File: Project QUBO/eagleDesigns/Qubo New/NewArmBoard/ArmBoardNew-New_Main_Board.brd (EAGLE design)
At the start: 114.3 x 114.3 mm, 13 parts, among them U1 BME280

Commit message: Prolly random fixes
I don't remember but it's probaly pretty good
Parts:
- moved JP1 7.66 mm to (20.3, 75.4)
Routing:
- net DGND: track 66.7 -> 59.6 mm
- net 5V: track 50.5 -> 47.6 mm
- added copper zone on layer 16, net N$1
- removed copper zone on layer 16, net DGND
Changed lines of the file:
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@@
 <text x="63.373" y="3.175" size="1.4224" layer="27" rot="R90">NC</text>
 <text x="65.786" y="3.175" size="1.4224" layer="27" rot="R90">NC</text>
-<text x="102.489" y="19.939" size="1.778" layer="21" rot="R90">ARM Shim Board
+<text x="34.925" y="19.431" size="1.778" layer="21" rot="R180">ARM Shim Board
 Rev 1.0
 Brendan Kane and Alex Jiao
 R@M 2018</text>
+<hole x="6.35" y="81.28" drill="3.302"/>
+<hole x="6.35" y="33.02" drill="3.302"/>
+<hole x="107.95" y="33.02" drill="3.302"/>
+<hole x="107.95" y="81.28" drill="3.302"/>
 </plain>
 <attributes>
@@
 <element name="R11" library="resistor" library_urn="urn:adsk.eagle:library:348" package="R0805" package3d_urn="urn:adsk.eagle:package:26059/1" value="5k" x="20.32" y="68.961"/>
 <element name="R17" library="resistor" library_urn="urn:adsk.eagle:library:348" package="R0805" package3d_urn="urn:adsk.eagle:package:26059/1" value="5k" x="84.709" y="42.799"/>
-<element name="JP1" library="pinhead" package="1X02" value="" x="12.7" y="76.2" rot="R90"/>
+<element name="JP1" library="pinhead" package="1X02" value="" x="20.32" y="75.438" rot="R90"/>
 </elements>
 <signals>
@@
 <wire x1="18.989" y1="60.706" x2="18.989" y2="57.023" width="0.254" layer="1"/>
 <wire x1="18.989" y1="57.023" x2="19.497" y2="56.515" width="0.254" layer="1"/>
-<wire x1="19.1465" y1="45.5625" x2="19.243" y2="45.466" width="0.254" layer="1"/>
 <wire x1="18.989" y1="49.657" x2="18.989" y2="45.72" width="0.254" layer="1"/>
-<wire x1="18.989" y1="45.72" x2="19.1465" y2="45.5625" width="0.254" layer="1"/>
+<wire x1="18.989" y1="45.72" x2="19.243" y2="45.466" width="0.254" layer="1"/>
 <wire x1="19.497" y1="56.515" x2="19.497" y2="50.165" width="0.254" layer="1"/>
 <wire x1="19.497" y1="50.165" x2="18.989" y2="49.657" width="0.254" layer="1"/>
@@
 <wire x1="20.50426875" y1="69.9904" x2="32.3716" y2="69.9904" width="0.254" layer="1"/>
 <wire x1="32.3716" y1="69.9904" x2="34.925" y2="67.437" width="0.254" layer="1"/>
-<wire x1="12.7" y1="74.93" x2="18.669" y2="68.961" width="0.254" layer="1"/>
 <wire x1="18.669" y1="68.961" x2="19.37" y2="68.961" width="0.254" layer="1"/>
 <polygon width="0.254" layer="1">
-<vertex x="6.604" y="76.2"/>
 <vertex x="12.7" y="70.104"/>
 <vertex x="12.7" y="38.1"/>
@@
 <vertex x="33.528" y="55.372"/>
 </polygon>
+<wire x1="19.37" y1="68.961" x2="19.37" y2="73.218" width="0.254" layer="1"/>
+<wire x1="19.37" y1="73.218" x2="20.32" y2="74.168" width="0.254" layer="1"/>
 </signal>
 <signal name="RES">
@@
 <contactref element="JP1" pad="2"/>
 <wire x1="50.8" y1="76.2976" x2="51.8886" y2="76.2976" width="0.254" layer="1"/>
-<polygon width="0.1524" layer="16">
-<vertex x="6.096" y="3.556"/>
-<vertex x="6.604" y="3.048"/>
-<vertex x="107.696" y="3.048"/>
-<vertex x="109.728" y="5.08"/>
-<vertex x="94.996" y="19.812"/>
-<vertex x="94.996" y="89.408"/>
-<vertex x="6.604" y="89.408"/>
-</polygon>
 <wire x1="50.8" y1="76.2976" x2="50.8" y2="78.232" width="0.254" layer="1"/>
 <wire x1="50.8" y1="78.232" x2="55.118" y2="78.232" width="0.254" layer="1"/>
@@
 <wire x1="68.58" y1="76.962" x2="55.118" y2="76.962" width="0.254" layer="1"/>
 <wire x1="33.4264" y1="66.3956" x2="34.925" y2="64.897" width="0.254" layer="16"/>
-<wire x1="31.50726875" y1="66.3956" x2="33.4264" y2="66.3956" width="0.254" layer="16"/>
-<wire x1="12.7" y1="77.47" x2="20.43286875" y2="77.47" width="0.254" layer="16"/>
-<wire x1="20.43286875" y1="77.47" x2="31.50726875" y2="66.3956" width="0.254" layer="16"/>
+<wire x1="33.4264" y1="66.3956" x2="31.50726875" y2="66.3956" width="0.254" layer="16"/>
+<wire x1="20.32" y1="76.708" x2="20.43286875" y2="77.47" width="0.254" layer="16"/>
 <wire x1="50.8" y1="76.2976" x2="48.3576" y2="76.2976" width="0.254" layer="1"/>
 <wire x1="48.3576" y1="76.2976" x2="48.26" y2="76.2" width="0.254" layer="1"/>
 <via x="48.26" y="76.2" extent="1-16" drill="0.35"/>
+<wire x1="31.50726875" y1="66.3956" x2="21.19486875" y2="76.708" width="0.254" layer="16"/>
+<wire x1="21.19486875" y1="76.708" x2="20.32" y2="76.708" width="0.254" layer="16"/>
+<wire x1="34.925" y1="64.897" x2="48.26" y2="76.2" width="0" layer="19" extent="1-1"/>
 </signal>
 <signal name="CANTX">
@@
 <contactref element="U$3" pad="2-2"/>
 </signal>
+<signal name="N$1">
+<polygon width="0.254" layer="16">
+<vertex x="12.7" y="76.2"/>
+<vertex x="13.462" y="6.604"/>
+<vertex x="89.662" y="6.604"/>
+<vertex x="90.424" y="7.366"/>
+<vertex x="90.424" y="77.216"/>
+<vertex x="88.9" y="78.74"/>
+<vertex x="16.002" y="78.74"/>
+<vertex x="13.462" y="76.2"/>
+</polygon>
+</signal>
 </signals>

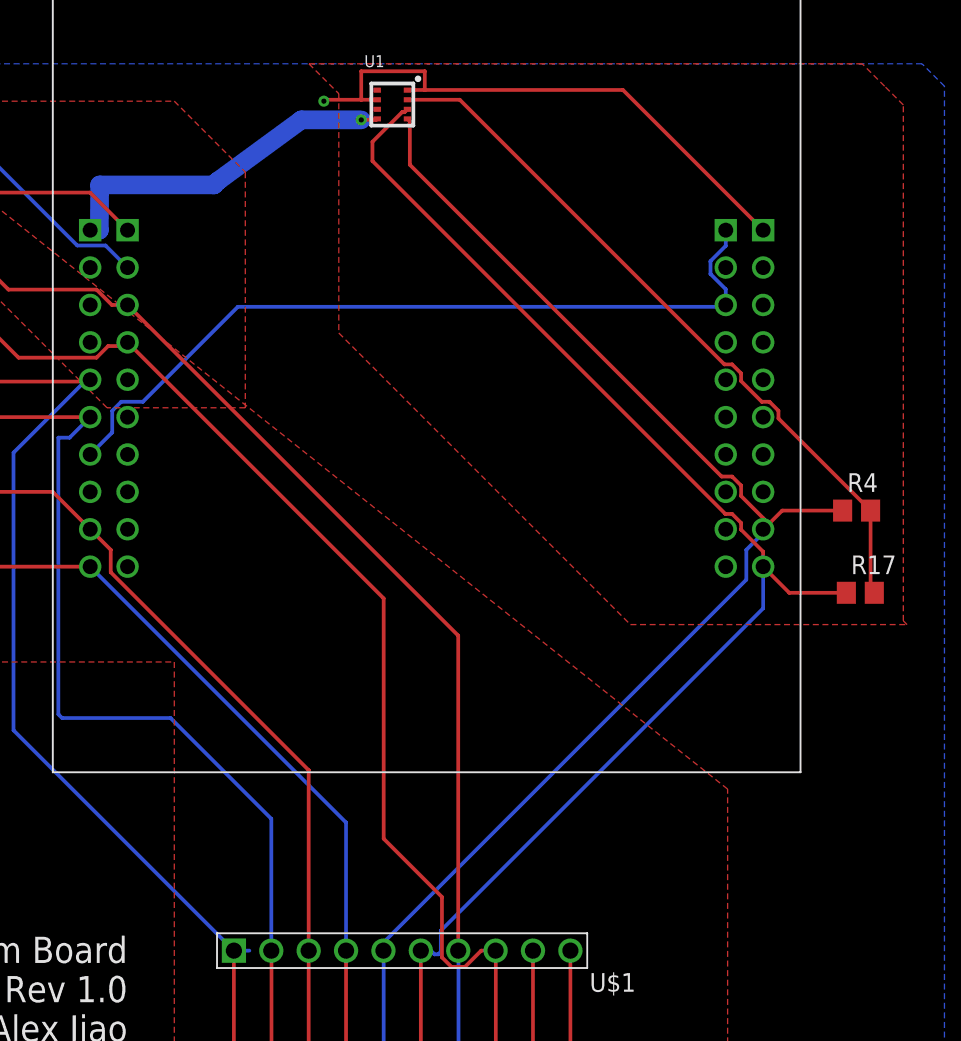
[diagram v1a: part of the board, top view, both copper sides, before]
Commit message: Fixes to TIVA board
Some of the pins were named wrong so I fixed them
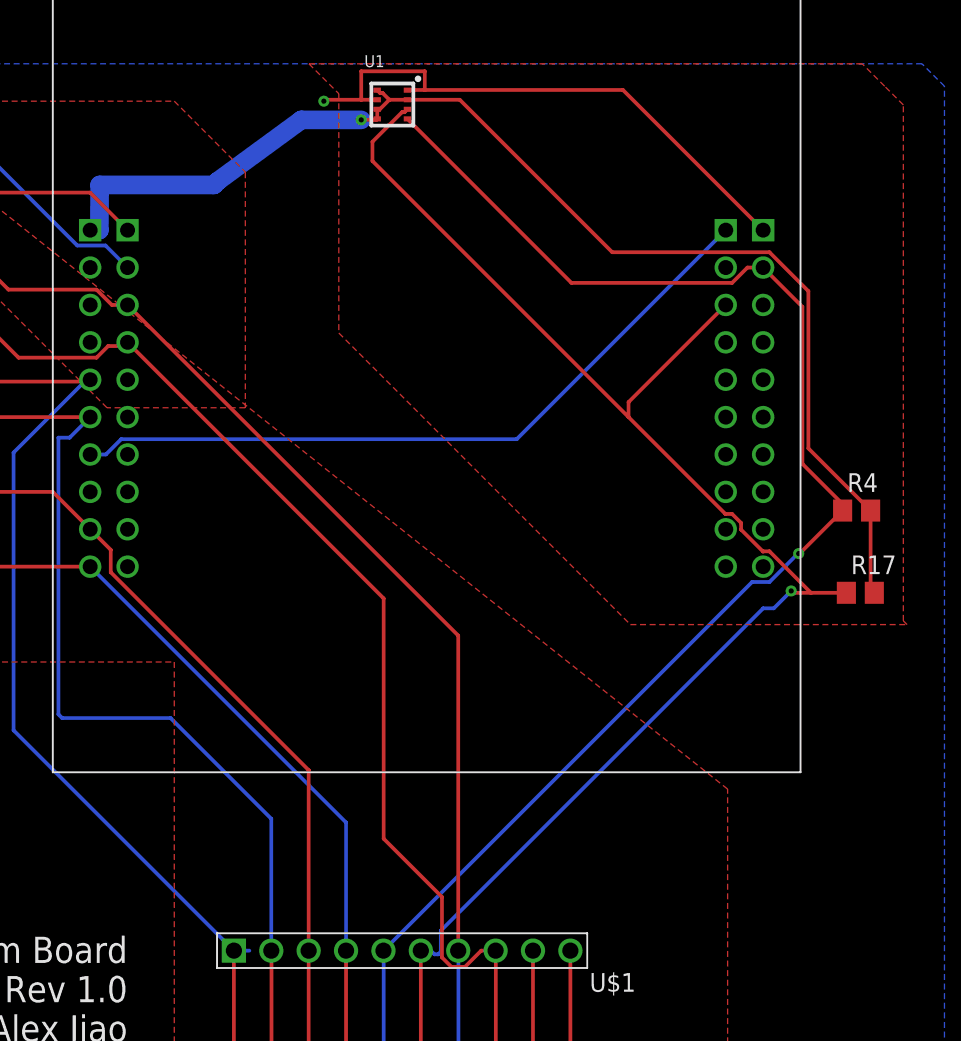
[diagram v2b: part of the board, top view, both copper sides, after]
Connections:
- net CANTX renamed CS
- net CTS_MF renamed MOSI_1
- net PB5 renamed CS_2
- net RTS_MF renamed MISO_1
- removed net PB2: U$3.2-2
- new net CS_0: U$3.2-9
- new net MISO_0: U$3.2-8
- new net MISO_3: U$3.3-5
- new net MOSI_0: U$3.1-8
- new net MOSI_3: U$3.3-6
- new net SCK_0: U$3.2-10
- net SCL_0: now also U$3.2-2; no longer U$3.2-9
- net SDA_0: now also U$3.4-3; no longer U$3.2-10
- net SPI_CLK: no longer U$3.4-3
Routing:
- net SDA_0: track 94.9 -> 105.7 mm, vias 0 -> 1
- net 3.3V: track 73.7 -> 83.5 mm
- net SCL_0: track 92.0 -> 100.0 mm, vias 0 -> 1
- net SPI_CLK: track 54.2 -> 49.5 mm
- added copper zone on layer 16, net DGND
- removed copper zone on layer 16, net N$1

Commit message: Changes to Tiva board
I had to rewire some things
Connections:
- new net SPI_CLK_2: U$3.1-7
- net 3.3V: now also R15.1, R16.1, U$1.P$9; no longer R17.2, R4.2
- net 5V: now also R17.2, R4.2; no longer R15.1, R16.1
- net N$9: no longer U$1.P$9
- net SCL_0: no longer U1.P$4
- net SCL_1: now also U1.P$4
- net SDA_0: no longer U1.P$3
- net SDA_1: now also U1.P$3
- net SPI_CLK: no longer U$3.1-7
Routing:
- net 3.3V: track 83.5 -> 180.6 mm, vias 1 -> 2
- net 5V: track 47.6 -> 109.2 mm
- net SPI_CLK: track 49.5 -> 0.00 mm
- net SDA_1: track 54.5 -> 101.0 mm, vias 0 -> 1
- net SCL_1: track 55.7 -> 94.1 mm, vias 0 -> 2
- net SCL_0: track 100.0 -> 70.8 mm
- net N$9: track 8.34 -> 0.02 mm
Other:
- board size 114.3 x 114.3 mm -> 114.3 x 88.9 mm
- board text added: "VV this side down VV"

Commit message: armboard modifications
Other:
- board size 114.3 x 88.9 mm -> 96.8 x 89.2 mm
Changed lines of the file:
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@@
 <?xml version="1.0" encoding="utf-8"?>
 <!DOCTYPE eagle SYSTEM "eagle.dtd">
-<eagle version="8.6.0">
+<eagle version="9.3.1">
 <drawing>
 <settings>
@@
 <text x="42.545" y="3.175" size="1.4224" layer="21" rot="R90">SCL_2</text>
 <wire x1="0" y1="88.9" x2="0" y2="0" width="0.1524" layer="20"/>
-<wire x1="0" y1="0" x2="114.3" y2="0" width="0.1524" layer="20"/>
-<wire x1="114.3" y1="0" x2="114.3" y2="88.9" width="0.1524" layer="20"/>
-<wire x1="114.3" y1="88.9" x2="0" y2="88.9" width="0.1524" layer="20"/>
+<wire x1="0" y1="0" x2="96.774" y2="-0.254" width="0.1524" layer="20"/>
+<wire x1="96.774" y1="-0.254" x2="96.774" y2="88.646" width="0.1524" layer="20"/>
+<wire x1="96.774" y1="88.646" x2="0" y2="88.9" width="0.1524" layer="20"/>
 <text x="45.085" y="3.175" size="1.4224" layer="21" rot="R90">SDA_2</text>
 <text x="47.752" y="3.175" size="1.4224" layer="21" rot="R90">SCL_1</text>
@@
 <hole x="6.35" y="81.28" drill="3.302"/>
 <hole x="6.35" y="33.02" drill="3.302"/>
-<hole x="107.95" y="33.02" drill="3.302"/>
-<hole x="107.95" y="81.28" drill="3.302"/>
-<text x="88.9" y="0" size="1.778" layer="121">VV this side down VV</text>
+<hole x="88.9" y="33.02" drill="3.302"/>
+<hole x="88.9" y="81.28" drill="3.302"/>
+<text x="63.5" y="0" size="1.778" layer="121">VV this side down VV</text>
 </plain>
 <attributes>
@@
 <param name="checkStop" value="0"/>
 <param name="checkValues" value="0"/>
+<param name="checkNames" value="1"/>
+<param name="checkWireStubs" value="1"/>
+<param name="checkPolygonWidth" value="0"/>
 <param name="useDiameter" value="13"/>
 <param name="maxErrors" value="50"/>
@@
 </autorouter>
 <elements>
-<element name="U1" library="BME280ComponentLibrary" package="BME280_LGA" value="BME280" x="52.9136" y="75.9726">
+<element name="U1" library="BME280ComponentLibrary" package="BME280_LGA" value="BME280" x="52.9136" y="75.9726" smashed="yes">
+<attribute name="NAME" x="51.0086" y="78.5126" size="0.8128" layer="25" font="vector"/>
 <attribute name="PROD_ID" value="IC-13090" x="52.9136" y="75.9726" size="1.778" layer="27" display="off"/>
+<attribute name="VALUE" x="51.0086" y="72.7976" size="0.8128" layer="27" font="vector"/>
 </element>
 <element name="U$1" library="molex" package="KK254_10-PIN" value="KK254_10-PIN" x="53.5787" y="18.488975" smashed="yes" rot="R180">
@@
 <attribute name="VALUE" x="66.294" y="12.7" size="1.27" layer="27" rot="R180"/>
 </element>
-<element name="U$3" library="texas" package="TIVA-C_EVAL" value="TIVA-C_EVAL" x="55.245" y="63.627"/>
-<element name="R13" library="resistor" library_urn="urn:adsk.eagle:library:348" package="R0805" package3d_urn="urn:adsk.eagle:package:26059/1" value="5k" x="20.447" y="56.515" rot="R180"/>
-<element name="R14" library="resistor" library_urn="urn:adsk.eagle:library:348" package="R0805" package3d_urn="urn:adsk.eagle:package:26059/1" value="5k" x="19.939" y="60.706" rot="R180"/>
-<element name="R15" library="resistor" library_urn="urn:adsk.eagle:library:348" package="R0805" package3d_urn="urn:adsk.eagle:package:26059/1" value="5k" x="19.939" y="49.657"/>
-<element name="R16" library="resistor" library_urn="urn:adsk.eagle:library:348" package="R0805" package3d_urn="urn:adsk.eagle:package:26059/1" value="5k" x="20.193" y="45.466"/>
-<element name="R4" library="resistor" library_urn="urn:adsk.eagle:library:348" package="R0805" package3d_urn="urn:adsk.eagle:package:26059/1" value="5k" x="84.455" y="48.387"/>
-<element name="R8" library="resistor" library_urn="urn:adsk.eagle:library:348" package="R0805" package3d_urn="urn:adsk.eagle:package:26059/1" value="5k" x="20.447" y="64.897"/>
-<element name="R11" library="resistor" library_urn="urn:adsk.eagle:library:348" package="R0805" package3d_urn="urn:adsk.eagle:package:26059/1" value="5k" x="20.32" y="68.961"/>
-<element name="R17" library="resistor" library_urn="urn:adsk.eagle:library:348" package="R0805" package3d_urn="urn:adsk.eagle:package:26059/1" value="5k" x="84.709" y="42.799"/>
-<element name="JP1" library="pinhead" package="1X02" value="" x="20.32" y="75.438" rot="R90"/>
+<element name="U$3" library="texas" package="TIVA-C_EVAL" value="TIVA-C_EVAL" x="55.245" y="63.627" smashed="yes">
+<attribute name="NAME" x="31.115" y="97.917" size="5.08" layer="25"/>
+<attribute name="VALUE" x="31.115" y="28.067" size="1.27" layer="27"/>
+</element>
+<element name="R13" library="resistor" library_urn="urn:adsk.eagle:library:348" package="R0805" package3d_urn="urn:adsk.eagle:package:26059/1" value="5k" x="20.447" y="56.515" smashed="yes" rot="R180">
+<attribute name="NAME" x="21.082" y="55.245" size="1.27" layer="25" rot="R180"/>
+<attribute name="VALUE" x="21.082" y="59.055" size="1.27" layer="27" rot="R180"/>
+</element>
+<element name="R14" library="resistor" library_urn="urn:adsk.eagle:library:348" package="R0805" package3d_urn="urn:adsk.eagle:package:26059/1" value="5k" x="19.939" y="60.706" smashed="yes" rot="R180">
+<attribute name="NAME" x="20.574" y="59.436" size="1.27" layer="25" rot="R180"/>
+<attribute name="VALUE" x="20.574" y="63.246" size="1.27" layer="27" rot="R180"/>
+</element>
+<element name="R15" library="resistor" library_urn="urn:adsk.eagle:library:348" package="R0805" package3d_urn="urn:adsk.eagle:package:26059/1" value="5k" x="19.939" y="49.657" smashed="yes">
+<attribute name="NAME" x="19.304" y="50.927" size="1.27" layer="25"/>
+<attribute name="VALUE" x="19.304" y="47.117" size="1.27" layer="27"/>
+</element>
+<element name="R16" library="resistor" library_urn="urn:adsk.eagle:library:348" package="R0805" package3d_urn="urn:adsk.eagle:package:26059/1" value="5k" x="20.193" y="45.466" smashed="yes">
+<attribute name="NAME" x="19.558" y="46.736" size="1.27" layer="25"/>
+<attribute name="VALUE" x="19.558" y="42.926" size="1.27" layer="27"/>
+</element>
+<element name="R4" library="resistor" library_urn="urn:adsk.eagle:library:348" package="R0805" package3d_urn="urn:adsk.eagle:package:26059/1" value="5k" x="84.455" y="48.387" smashed="yes">
+<attribute name="NAME" x="83.82" y="49.657" size="1.27" layer="25"/>
+<attribute name="VALUE" x="83.82" y="45.847" size="1.27" layer="27"/>
+</element>
+<element name="R8" library="resistor" library_urn="urn:adsk.eagle:library:348" package="R0805" package3d_urn="urn:adsk.eagle:package:26059/1" value="5k" x="20.447" y="64.897" smashed="yes">
+<attribute name="NAME" x="19.812" y="66.167" size="1.27" layer="25"/>
+<attribute name="VALUE" x="19.812" y="62.357" size="1.27" layer="27"/>
+</element>
+<element name="R11" library="resistor" library_urn="urn:adsk.eagle:library:348" package="R0805" package3d_urn="urn:adsk.eagle:package:26059/1" value="5k" x="20.32" y="68.961" smashed="yes">
+<attribute name="NAME" x="19.685" y="70.231" size="1.27" layer="25"/>
+<attribute name="VALUE" x="19.685" y="66.421" size="1.27" layer="27"/>
+</element>
+<element name="R17" library="resistor" library_urn="urn:adsk.eagle:library:348" package="R0805" package3d_urn="urn:adsk.eagle:package:26059/1" value="5k" x="84.709" y="42.799" smashed="yes">
+<attribute name="NAME" x="84.074" y="44.069" size="1.27" layer="25"/>
+<attribute name="VALUE" x="84.074" y="40.259" size="1.27" layer="27"/>
+</element>
+<element name="JP1" library="pinhead" package="1X02" value="" x="20.32" y="75.438" smashed="yes" rot="R90">
+<attribute name="NAME" x="18.4912" y="72.8218" size="1.27" layer="25" ratio="10" rot="R90"/>
+<attribute name="VALUE" x="23.495" y="72.898" size="1.27" layer="27" rot="R90"/>
+</element>
 </elements>
 <signals>
@@
 <wire x1="33.00586875" y1="67.437" x2="33.03126875" y2="70.5104" width="1.27" layer="16"/>
 <wire x1="41.0464" y1="70.7644" x2="46.736" y2="74.93" width="1.27" layer="16"/>
-<polygon width="0.254" layer="1">
-<vertex x="87.884" y="40.64"/>
-<vertex x="87.63" y="40.894"/>
-<vertex x="87.63" y="55.88"/>
-</polygon>
 <wire x1="51.821" y1="74.93" x2="51.816" y2="74.93" width="0.254" layer="1"/>
 <wire x1="51.816" y1="74.93" x2="50.8" y2="74.93" width="0.254" layer="1"/>
@@
 </signal>
 </signals>
+<mfgpreviewcolors>
+<mfgpreviewcolor name="soldermaskcolor" color="0xC8008000"/>
+<mfgpreviewcolor name="silkscreencolor" color="0xFFFEFEFE"/>
+<mfgpreviewcolor name="backgroundcolor" color="0xFF282828"/>
+<mfgpreviewcolor name="coppercolor" color="0xFFFFBF00"/>
+<mfgpreviewcolor name="substratecolor" color="0xFF786E46"/>
+</mfgpreviewcolors>
 <errors>
 </errors>
